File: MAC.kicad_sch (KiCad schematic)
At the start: 12 parts, among them U6 Opamp_Dual, U7 Opamp_Dual

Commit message: last TH mounting board
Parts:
- removed C11: C, symbol Device:C
- removed D10: DIODE, symbol Simulation_SPICE:DIODE
- removed R12, R14, R15: R, symbol Device:R
- removed U6, U7: Opamp_Dual, symbol Device:Opamp_Dual
- added U9: LM358, symbol Amplifier_Operational:LM358
- C39: renamed from C10; value C -> 0.1uF; footprint (none) -> Capacitor_SMD:C_0603_1608Metric
- D9: value DIODE -> S1K-13-F; footprint (none) -> Diode_SMD:D_SMA
- R18: renamed from R13; value R -> 10k; footprint (none) -> Resistor_SMD:R_0603_1608Metric
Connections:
- net GNDREF is gone; now on net GND: A1.29 (GND), A1.4 (GND), C39.1, D9.1 (A)
- net Ain: now also R18.2
- net Vunreg+: now also U9.4 (V-)
- net Vunreg-: now also U9.8 (V+)
- net GND: now reaches DS1.1 (GND), DS1.30 (GND)
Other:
- moved on the sheet: A1, C39, D9, DS1, R18

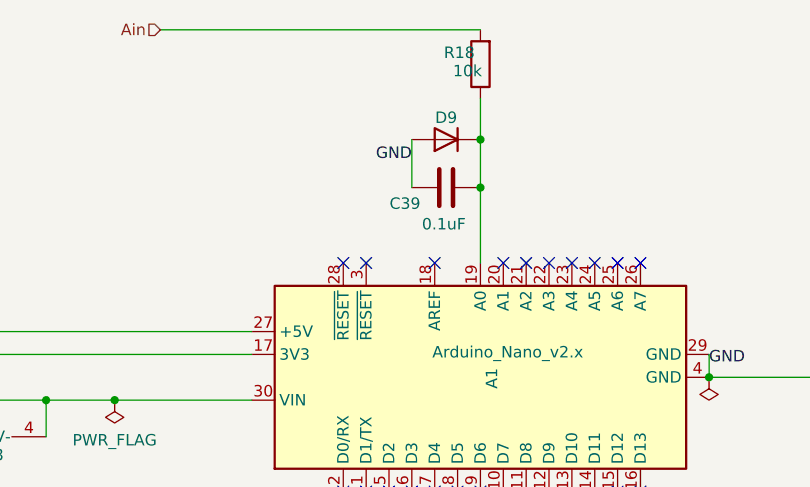
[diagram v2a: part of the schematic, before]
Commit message: all SMD components going into boards
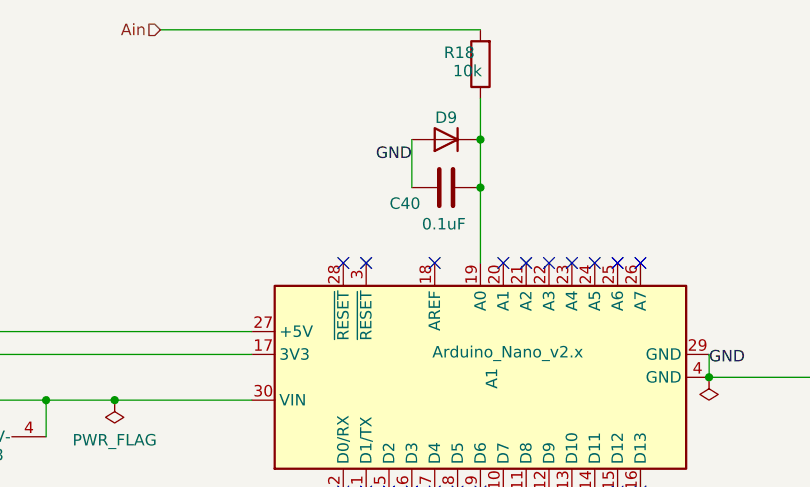
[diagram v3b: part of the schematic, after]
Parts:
- U9: footprint (none) -> Package_TO_SOT_SMD:SOT-223-8
- renumbered C39 to C40
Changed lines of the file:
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@@
   (symbol (lib_id "Device:C") (at 137.16 79.502 90) (unit 1)
     (in_bom yes) (on_board yes)
-    (property "Reference" "C39" (id 0) (at 132.588 81.28 90))
+    (property "Reference" "C40" (id 0) (at 132.588 81.28 90))
     (property "Value" "0.1uF" (id 1) (at 136.906 83.566 90))
     (property "Footprint" "Capacitor_SMD:C_0603_1608Metric" (id 2) (at 140.97 78.5368 0)
@@
     (property "Reference" "U9" (id 0) (at 85.852 111.252 90))
     (property "Value" "LM358" (id 1) (at 85.09 109.22 90))
-    (property "Footprint" "" (id 2) (at 85.09 104.648 0)
+    (property "Footprint" "Package_TO_SOT_SMD:SOT-223-8" (id 2) (at 85.09 104.648 0)
       (effects (font (size 1.27 1.27)) hide)
     )

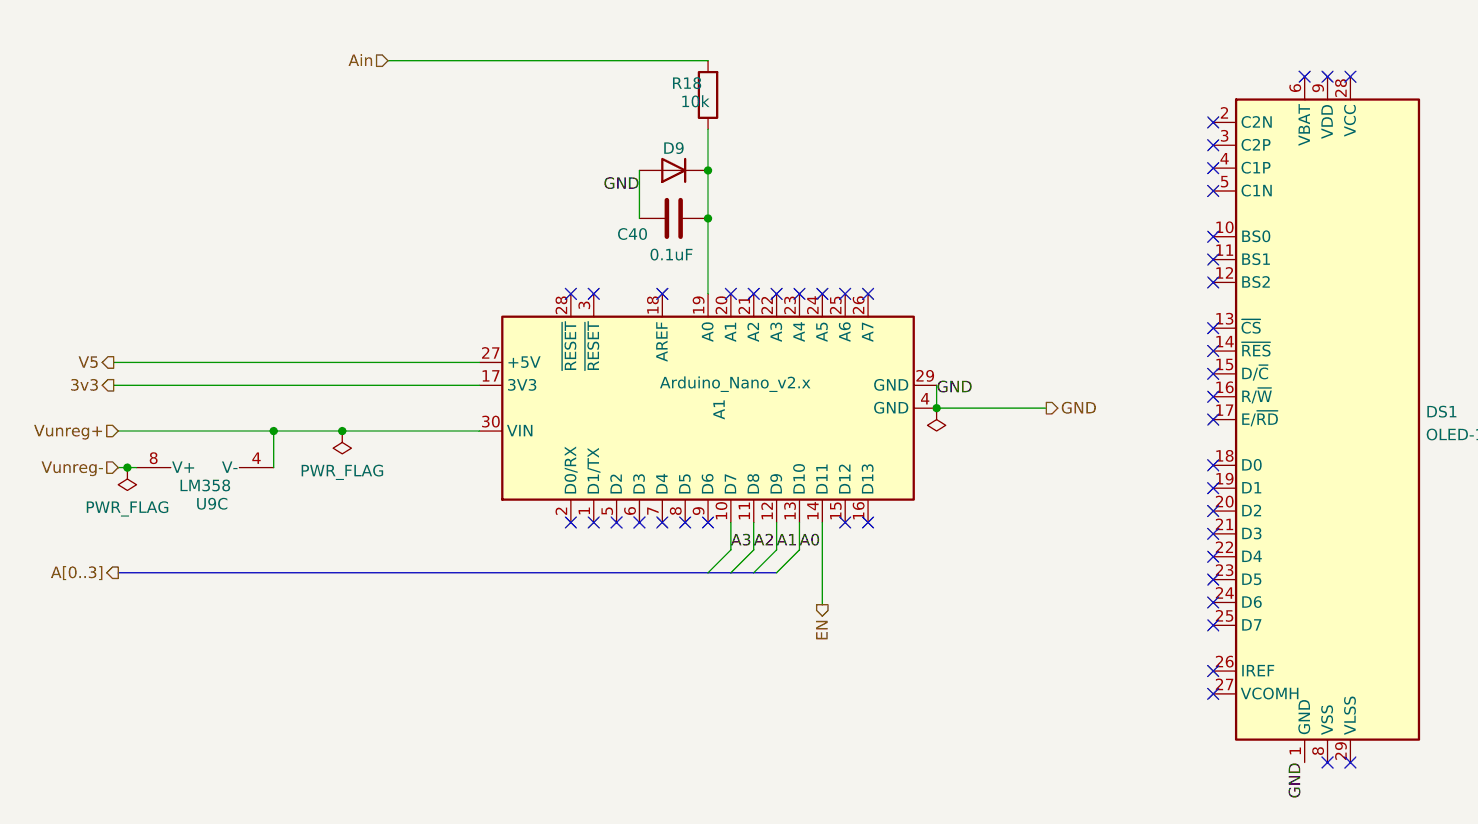
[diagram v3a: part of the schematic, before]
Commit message: new board with SMD
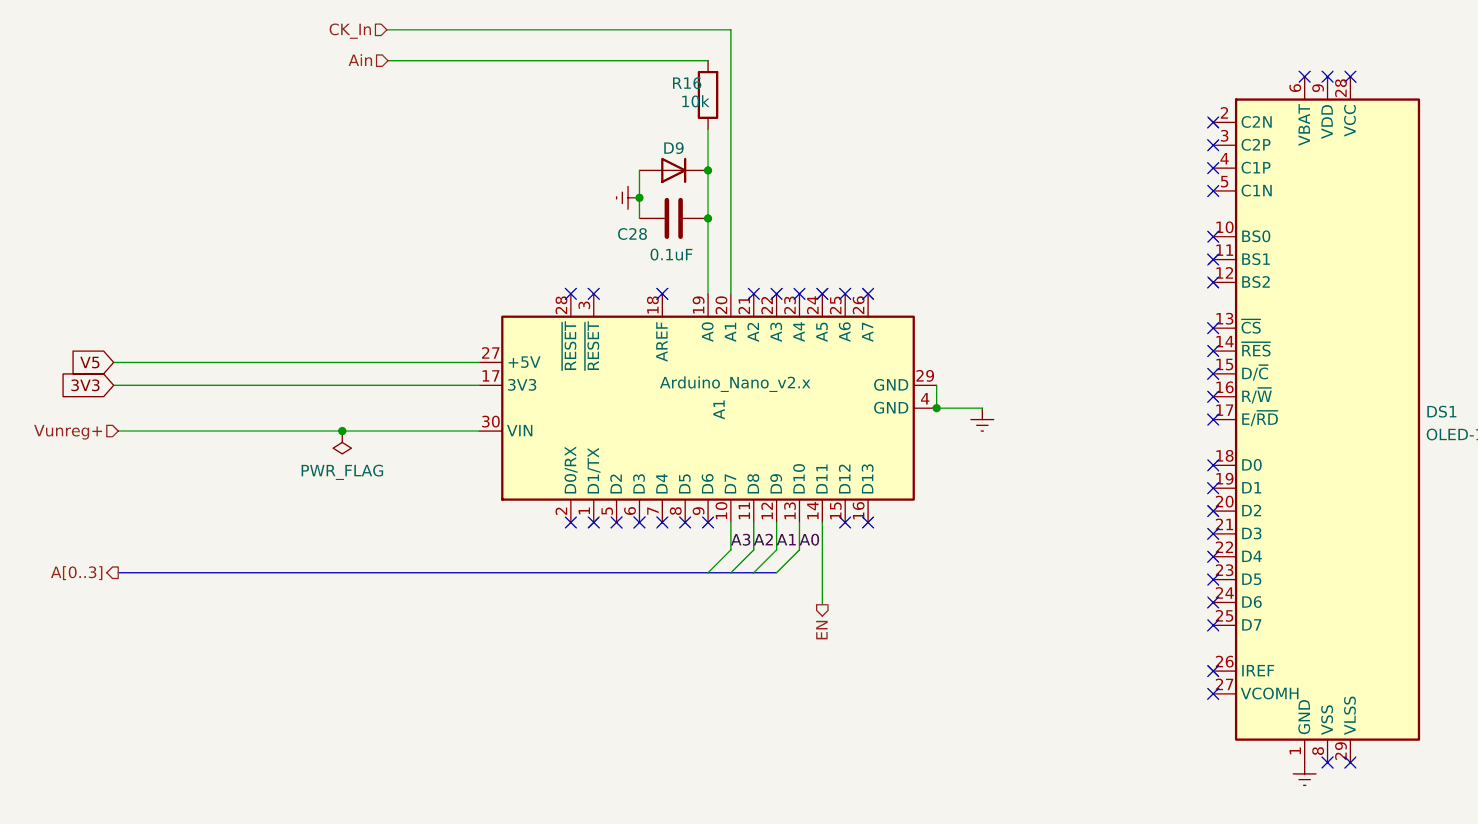
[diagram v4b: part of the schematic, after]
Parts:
- removed U9: LM358, Package_TO_SOT_SMD:SOT-223-8, symbol Amplifier_Operational:LM358
- renumbered C40 to C28, R18 to R16
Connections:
- net CK_In: now reaches A1.20 (A1)
- net 3v3 renamed 3V3
- net GND renamed GNDREF
- no-connect marks 46 -> 45
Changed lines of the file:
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@@
 (kicad_sch (version 20211123) (generator eeschema)
   (paper "A4")
-  (junction (at 92.71 103.124) (diameter 0) (color 0 0 0 0)
-  )
   (junction (at 100.33 103.124) (diameter 0) (color 0 0 0 0)
   )
-  (junction (at 76.454 107.188) (diameter 0) (color 0 0 0 0)
-  )
   (junction (at 166.37 100.584) (diameter 0) (color 0 0 0 0)
   )
+  (junction (at 133.35 77.216) (diameter 0) (color 0 0 0 0)
+  )
   (junction (at 140.97 79.502) (diameter 0) (color 0 0 0 0)
   )
   (junction (at 140.97 74.168) (diameter 0) (color 0 0 0 0)
   )
-  (no_connect (at 143.51 87.884))
   (no_connect (at 212.344 63.754))
   (no_connect (at 209.804 63.754))
@@
     (stroke (width 0) (type default) (color 0 0 0 0))
   )
-  (wire (pts (xy 92.71 107.188) (xy 92.71 103.124))
-    (stroke (width 0) (type default) (color 0 0 0 0))
-  )
   (wire (pts (xy 140.97 74.168) (xy 140.97 79.502))
     (stroke (width 0) (type default) (color 0 0 0 0))
   )
+  (wire (pts (xy 143.51 87.884) (xy 143.51 58.547))
+    (stroke (width 0) (type default) (color 0 0 0 0))
+  )
   (wire (pts (xy 166.37 98.044) (xy 166.37 100.584))
     (stroke (width 0) (type default) (color 0 0 0 0))
@@
     (stroke (width 0) (type default) (color 0 0 0 0))
   )
-  (wire (pts (xy 75.438 107.188) (xy 76.454 107.188))
-    (stroke (width 0) (type default) (color 0 0 0 0))
-  )
   (bus (pts (xy 75.438 118.872) (xy 140.97 118.872))
     (stroke (width 0) (type default) (color 0 0 0 0))
   )
-  (wire (pts (xy 133.35 74.168) (xy 133.35 79.502))
+  (wire (pts (xy 133.35 77.216) (xy 133.35 79.502))
+    (stroke (width 0) (type default) (color 0 0 0 0))
+  )
+  (wire (pts (xy 133.35 74.168) (xy 133.35 77.216))
+    (stroke (width 0) (type default) (color 0 0 0 0))
+  )
+  (wire (pts (xy 143.51 58.547) (xy 105.283 58.547))
     (stroke (width 0) (type default) (color 0 0 0 0))
   )
@@
     (stroke (width 0) (type default) (color 0 0 0 0))
   )
-  (wire (pts (xy 166.37 100.584) (xy 178.562 100.584))
+  (wire (pts (xy 166.37 100.584) (xy 171.45 100.584))
     (stroke (width 0) (type default) (color 0 0 0 0))
   )
@@
     (stroke (width 0) (type default) (color 0 0 0 0))
   )
-  (wire (pts (xy 75.438 103.124) (xy 92.71 103.124))
-    (stroke (width 0) (type default) (color 0 0 0 0))
-  )
-  (wire (pts (xy 92.71 103.124) (xy 100.33 103.124))
-    (stroke (width 0) (type default) (color 0 0 0 0))
-  )
-  (wire (pts (xy 76.454 107.188) (xy 77.47 107.188))
+  (wire (pts (xy 75.438 103.124) (xy 100.33 103.124))
     (stroke (width 0) (type default) (color 0 0 0 0))
   )
@@
     (effects (font (size 1.27 1.27)) (justify left bottom))
   )
-  (label "GND" (at 207.264 139.954 270)
-    (effects (font (size 1.27 1.27)) (justify right bottom))
-  )
   (label "A0" (at 151.13 116.332 0)
     (effects (font (size 1.27 1.27)) (justify left bottom))
   )
-  (label "GND" (at 133.35 76.708 180)
-    (effects (font (size 1.27 1.27)) (justify right bottom))
-  )
   (label "A1" (at 148.59 116.332 0)
     (effects (font (size 1.27 1.27)) (justify left bottom))
@@
     (effects (font (size 1.27 1.27)) (justify left bottom))
   )
-  (label "GND" (at 166.37 99.314 0)
-    (effects (font (size 1.27 1.27)) (justify left bottom))
+  (global_label "3V3" (shape input) (at 74.93 98.044 180) (fields_autoplaced)
+    (effects (font (size 1.27 1.27)) (justify right))
+    (property "Intersheet References" "${INTERSHEET_REFS}" (id 0) (at 69.0982 97.9646 0)
+      (effects (font (size 1.27 1.27)) (justify right))
+    )
+  )
+  (global_label "V5" (shape input) (at 74.93 95.504 180) (fields_autoplaced)
+    (effects (font (size 1.27 1.27)) (justify right))
+    (property "Intersheet References" "${INTERSHEET_REFS}" (id 0) (at 70.3077 95.4246 0)
+      (effects (font (size 1.27 1.27)) (justify right))
+    )
   )
   (hierarchical_label "EN" (shape output) (at 153.67 122.428 270)
     (effects (font (size 1.27 1.27)) (justify right))
   )
-  (hierarchical_label "3v3" (shape output) (at 74.93 98.044 180)
+  (hierarchical_label "CK_In" (shape input) (at 105.283 58.547 180)
     (effects (font (size 1.27 1.27)) (justify right))
   )
@@
     (effects (font (size 1.27 1.27)) (justify right))
   )
-  (hierarchical_label "V5" (shape output) (at 74.93 95.504 180)
-    (effects (font (size 1.27 1.27)) (justify right))
-  )
   (hierarchical_label "Ain" (shape input) (at 105.41 61.976 180)
-    (effects (font (size 1.27 1.27)) (justify right))
-  )
-  (hierarchical_label "GND" (shape output) (at 178.562 100.584 0)
-    (effects (font (size 1.27 1.27)) (justify left))
-  )
-  (hierarchical_label "Vunreg-" (shape input) (at 75.438 107.188 180)
     (effects (font (size 1.27 1.27)) (justify right))
   )
   (symbol (lib_id "Device:R") (at 140.97 65.786 180) (unit 1)
     (in_bom yes) (on_board yes)
-    (property "Reference" "R18" (id 0) (at 136.906 64.516 0)
+    (property "Reference" "R16" (id 0) (at 136.906 64.516 0)
       (effects (font (size 1.27 1.27)) (justify right))
     )
@@
     (pin "2")
   )
-  (symbol (lib_id "power:PWR_FLAG") (at 76.454 107.188 180) (unit 1)
-    (in_bom yes) (on_board yes) (fields_autoplaced)
-    (property "Reference" "#FLG013" (id 0) (at 76.454 109.093 0)
-      (effects (font (size 1.27 1.27)) hide)
-    )
-    (property "Value" "PWR_FLAG" (id 1) (at 76.454 111.6314 0))
-    (property "Footprint" "" (id 2) (at 76.454 107.188 0)
-      (effects (font (size 1.27 1.27)) hide)
-    )
-    (property "Datasheet" "~" (id 3) (at 76.454 107.188 0)
-      (effects (font (size 1.27 1.27)) hide)
-    )
-    (pin "1")
-  )
   (symbol (lib_id "power:PWR_FLAG") (at 100.33 103.124 180) (unit 1)
     (in_bom yes) (on_board yes) (fields_autoplaced)
-    (property "Reference" "#FLG012" (id 0) (at 100.33 105.029 0)
+    (property "Reference" "#FLG09" (id 0) (at 100.33 105.029 0)
       (effects (font (size 1.27 1.27)) hide)
     )
@@
     (pin "1")
   )
-  (symbol (lib_id "power:PWR_FLAG") (at 166.37 100.584 180) (unit 1)
-    (in_bom yes) (on_board yes) (fields_autoplaced)
-    (property "Reference" "#FLG011" (id 0) (at 166.37 102.489 0)
-      (effects (font (size 1.27 1.27)) hide)
-    )
-    (property "Value" "PWR_FLAG" (id 1) (at 166.37 105.0274 0)
-      (effects (font (size 1.27 1.27)) hide)
-    )
-    (property "Footprint" "" (id 2) (at 166.37 100.584 0)
-      (effects (font (size 1.27 1.27)) hide)
-    )
-    (property "Datasheet" "~" (id 3) (at 166.37 100.584 0)
+  (symbol (lib_id "power:GNDREF") (at 171.45 100.584 0) (unit 1)
+    (in_bom yes) (on_board yes) (fields_autoplaced)
+    (property "Reference" "#PWR025" (id 0) (at 171.45 106.934 0)
+      (effects (font (size 1.27 1.27)) hide)
+    )
+    (property "Value" "GNDREF" (id 1) (at 171.45 105.0274 0)
+      (effects (font (size 1.27 1.27)) hide)
+    )
+    (property "Footprint" "" (id 2) (at 171.45 100.584 0)
+      (effects (font (size 1.27 1.27)) hide)
+    )
+    (property "Datasheet" "" (id 3) (at 171.45 100.584 0)
       (effects (font (size 1.27 1.27)) hide)
     )
@@
   (symbol (lib_id "Device:C") (at 137.16 79.502 90) (unit 1)
     (in_bom yes) (on_board yes)
-    (property "Reference" "C40" (id 0) (at 132.588 81.28 90))
+    (property "Reference" "C28" (id 0) (at 132.588 81.28 90))
     (property "Value" "0.1uF" (id 1) (at 136.906 83.566 90))
     (property "Footprint" "Capacitor_SMD:C_0603_1608Metric" (id 2) (at 140.97 78.5368 0)
@@
     (pin "9")
   )
-  (symbol (lib_id "Amplifier_Operational:LM358") (at 85.09 104.648 90) (unit 3)
-    (in_bom yes) (on_board yes)
-    (property "Reference" "U9" (id 0) (at 85.852 111.252 90))
-    (property "Value" "LM358" (id 1) (at 85.09 109.22 90))
-    (property "Footprint" "Package_TO_SOT_SMD:SOT-223-8" (id 2) (at 85.09 104.648 0)
-      (effects (font (size 1.27 1.27)) hide)
-    )
-    (property "Datasheet" "http://www.ti.com/lit/ds/symlink/lm2904-n.pdf" (id 3) (at 85.09 104.648 0)
-      (effects (font (size 1.27 1.27)) hide)
-    )
-    (pin "1")
-    (pin "2")
-    (pin "3")
-    (pin "5")
-    (pin "6")
-    (pin "7")
-    (pin "4")
-    (pin "8")
+  (symbol (lib_id "power:GNDREF") (at 207.264 139.954 0) (unit 1)
+    (in_bom yes) (on_board yes) (fields_autoplaced)
+    (property "Reference" "#PWR026" (id 0) (at 207.264 146.304 0)
+      (effects (font (size 1.27 1.27)) hide)
+    )
+    (property "Value" "GNDREF" (id 1) (at 207.264 144.3974 0)
+      (effects (font (size 1.27 1.27)) hide)
+    )
+    (property "Footprint" "" (id 2) (at 207.264 139.954 0)
+      (effects (font (size 1.27 1.27)) hide)
+    )
+    (property "Datasheet" "" (id 3) (at 207.264 139.954 0)
+      (effects (font (size 1.27 1.27)) hide)
+    )
+    (pin "1")
+  )
+  (symbol (lib_id "power:GNDREF") (at 133.35 77.216 270) (unit 1)
+    (in_bom yes) (on_board yes) (fields_autoplaced)
+    (property "Reference" "#PWR024" (id 0) (at 127 77.216 0)
+      (effects (font (size 1.27 1.27)) hide)
+    )
+    (property "Value" "GNDREF" (id 1) (at 128.9066 77.216 0)
+      (effects (font (size 1.27 1.27)) hide)
+    )
+    (property "Footprint" "" (id 2) (at 133.35 77.216 0)
+      (effects (font (size 1.27 1.27)) hide)
+    )
+    (property "Datasheet" "" (id 3) (at 133.35 77.216 0)
+      (effects (font (size 1.27 1.27)) hide)
+    )
+    (pin "1")
   )
 )
